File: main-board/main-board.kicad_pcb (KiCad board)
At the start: 2 copper layers, 89.8 x 61.6 mm, 62 parts, among them J1 16-bit, J2 7-12V, Q11 MBT3904DW1, Q12 MBT3904DW1, Q13 MBT3904DW1, Q14 MBT3904DW1, Q15 MBT3904DW1, Q16 MBT3904DW1, Q17 MBT3904DW1, Q18 MBT3904DW1, U1 CD40106BM96, U2 CD4024BM96, U3 CD4040BNSR, U4 27C256, U5 CD4028BM96, U6 KA78M05_TO252

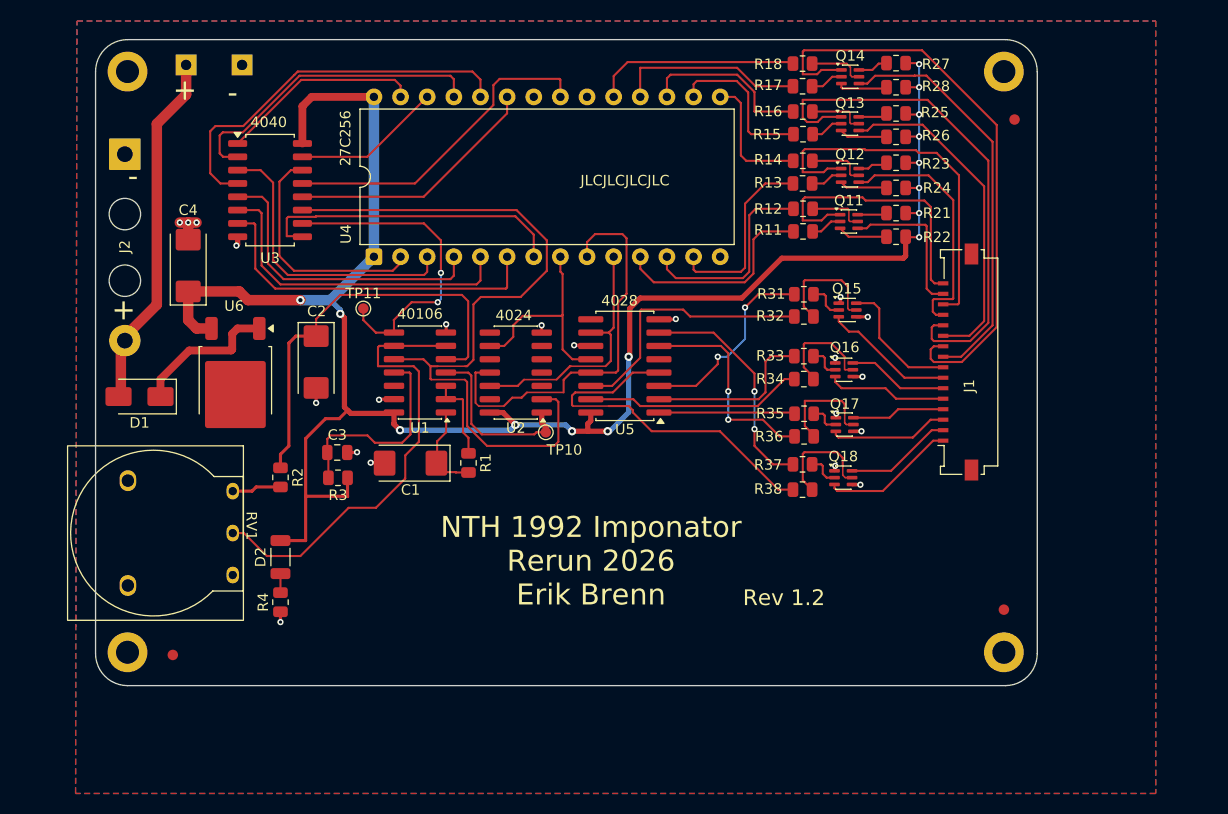
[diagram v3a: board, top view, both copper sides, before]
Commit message: new biasing and fixed footprints, shrinked pcb
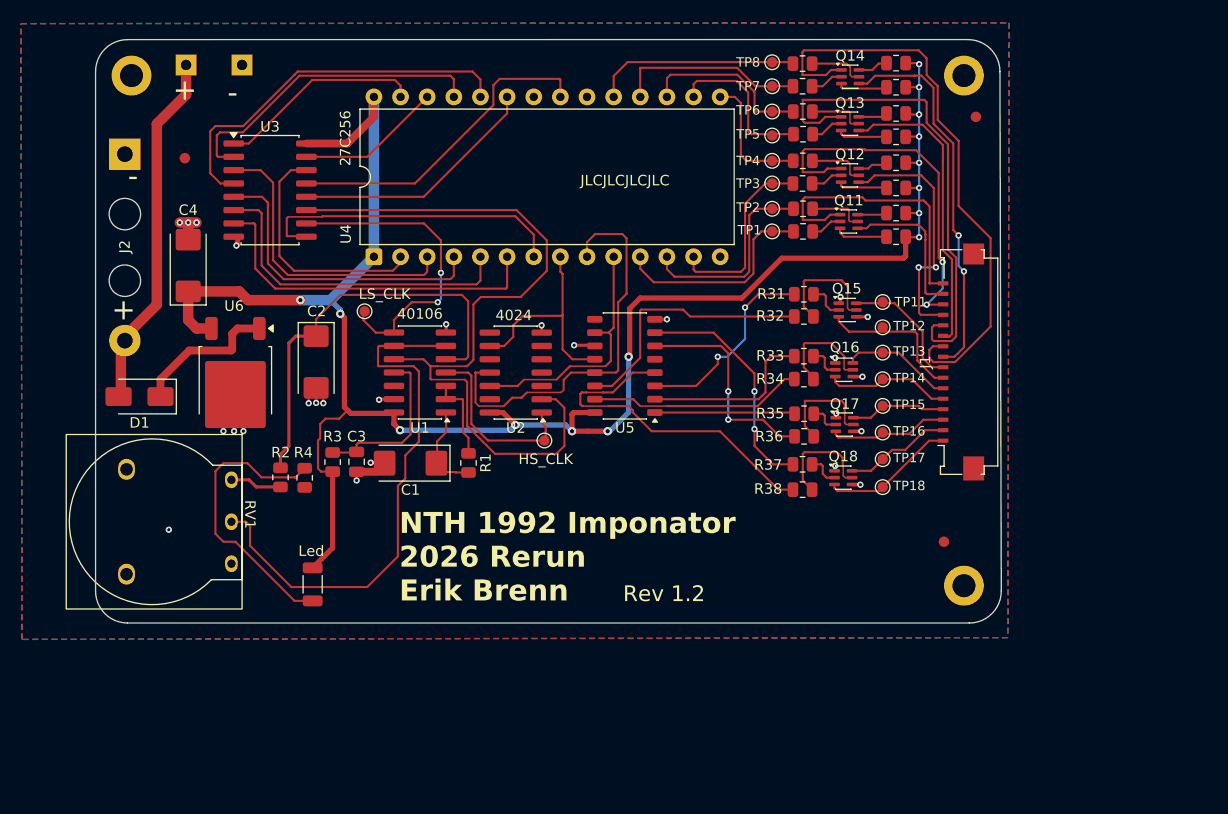
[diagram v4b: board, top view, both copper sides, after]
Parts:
- removed MH4: M3, MountingHole:MountingHole_2.2mm_M2_DIN965_Pad
- removed TP10: TestPoint, kicad-ezee-footprints:TestPoint_Pad_D1.0mm
- added TP1: TestPoint_Small, TestPoint:TestPoint_Pad_D1.0mm, F.Cu at (164.1, 75.9)
- added TP12: TestPoint_Small, TestPoint:TestPoint_Pad_D1.0mm, F.Cu at (174.6, 85.1)
- added TP13: TestPoint_Small, TestPoint:TestPoint_Pad_D1.0mm, F.Cu at (174.6, 87.5)
- added TP14: TestPoint_Small, TestPoint:TestPoint_Pad_D1.0mm, F.Cu at (174.6, 90.0)
- added TP15: TestPoint_Small, TestPoint:TestPoint_Pad_D1.0mm, F.Cu at (174.6, 92.6)
- added TP16: TestPoint_Small, TestPoint:TestPoint_Pad_D1.0mm, F.Cu at (174.6, 95.1)
- added TP17: TestPoint_Small, TestPoint:TestPoint_Pad_D1.0mm, F.Cu at (174.6, 97.7)
- added TP18: TestPoint_Small, TestPoint:TestPoint_Pad_D1.0mm, F.Cu at (174.6, 100.3)
- added TP2: TestPoint_Small, TestPoint:TestPoint_Pad_D1.0mm, F.Cu at (164.1, 73.8)
- added TP3: TestPoint_Small, TestPoint:TestPoint_Pad_D1.0mm, F.Cu at (164.1, 71.4)
- added TP4: TestPoint_Small, TestPoint:TestPoint_Pad_D1.0mm, F.Cu at (164.1, 69.2)
- added TP5: TestPoint_Small, TestPoint:TestPoint_Pad_D1.0mm, F.Cu at (164.1, 66.8)
- added TP50: HS_CLK, kicad-ezee-footprints:TestPoint_Pad_D1.0mm, F.Cu at (142.4, 95.9)
- added TP51: LS_CLK, kicad-ezee-footprints:TestPoint_Pad_D1.0mm, F.Cu at (125.2, 83.6)
- added TP6: TestPoint_Small, TestPoint:TestPoint_Pad_D1.0mm, F.Cu at (164.1, 64.5)
- added TP7: TestPoint_Small, TestPoint:TestPoint_Pad_D1.0mm, F.Cu at (164.1, 62.1)
- added TP8: TestPoint_Small, TestPoint:TestPoint_Pad_D1.0mm, F.Cu at (164.1, 59.8)
- D2: value LED -> Led
- J1: footprint Connector_FFC-FPC:Molex_200528-0160_1x16-1MP_P1.00mm_Horizontal -> kicad-ezee-footprints:FPC_1x16-P1.00mm_Horizontal
- R11, R12, R13, R14, R15, R16, R17, R18: value 8.2k -> 20k
- R21, R22, R23, R24, R25, R26, R27, R28: value 120 -> 270
- R31, R32, R33, R34, R35, R36, R37, R38: value 2.7k -> 5.2k
- TP11: value TestPoint -> TestPoint_Small; footprint kicad-ezee-footprints:TestPoint_Pad_D1.0mm -> TestPoint:TestPoint_Pad_D1.0mm
- U3: footprint Package_SO:SOP-16_4.4x10.4mm_P1.27mm -> Package_SO:SO-16_5.3x10.2mm_P1.27mm
- U5: footprint Package_SO:SOIC-16W_5.3x10.2mm_P1.27mm -> Package_SO:JEITA_SOIC-16_3.9x9.9mm_P1.27mm
- moved MH2 96.9 mm to (182.4, 61.1)
- moved TP11 49.5 mm to (174.6, 82.7)
- moved FID3 47.4 mm to (108.1, 69.0)
- moved R4 12.1 mm to (119.5, 99.4)
- moved FID2 8.64 mm to (180.5, 105.5)
- moved MH3 7.41 mm to (182.4, 109.7)
- moved D2 4.02 mm to (120.3, 109.6)
- moved FID1 3.69 mm to (183.5, 65.0)
- moved C3 2.05 mm to (124.5, 97.9), turned to -90 degrees
- moved R3 1.58 mm to (122.2, 97.9), turned to 90 degrees
- moved RV1 1.09 mm to (112.5, 99.6)
- moved MH1 0.54 mm to (103.0, 61.1)
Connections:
- net Net-(U2-Q0) renamed /A0
- net Net-(U2-Q1) renamed /A1
- net Net-(U2-Q2) renamed /A2
- net Net-(U2-~{CLK}) renamed /HS_CLK
- net Net-(U3-Q0) renamed /A3
- net Net-(U3-Q1) renamed /A4
- net Net-(U3-Q10) renamed /A13
- net Net-(U3-Q11) renamed /A15
- net Net-(U3-Q2) renamed /A5
- net Net-(U3-Q3) renamed /A6
- net Net-(U3-Q4) renamed /A7
- net Net-(U3-Q5) renamed /A8
- net Net-(U3-Q6) renamed /A9
- net Net-(U3-Q7) renamed /A10
- net Net-(U3-Q8) renamed /A11
- net Net-(U3-Q9) renamed /A12
- TP11 pad 1: Net-(U3-CLK) -> O1
- U1 pad 8: Net-(U3-CLK) -> /LS_CLK
- U3 pad 10: Net-(U3-CLK) -> /LS_CLK
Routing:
- net Net-(U3-CLK): track 30.5 -> 0.00 mm, vias 2 -> 0
- net /LS_CLK: track 0.00 -> 30.5 mm, vias 0 -> 2
- net Net-(D2-K): track 1.81 -> 27.7 mm
- net GND: track 20.7 -> 36.7 mm, vias 21 -> 26
- net Net-(RV1-Pad2): track 43.6 -> 51.7 mm
- net Net-(C3-Pad1): track 19.9 -> 16.0 mm
- net I6: track 32.0 -> 28.4 mm
- net I5: track 49.8 -> 46.3 mm
- net +5V: track 186.7 -> 183.3 mm
- net I8: track 39.1 -> 36.2 mm, vias 0 -> 2
- net Net-(U2-MR): track 73.3 -> 75.0 mm
- net Net-(U5-S7): track 34.6 -> 33.1 mm
- net O2: track 12.6 -> 14.1 mm
- net 03: track 9.61 -> 10.7 mm
- net /HS_CLK: track 16.8 -> 17.7 mm
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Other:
- board size 89.8 x 61.6 mm -> 86.4 x 55.6 mm
- board text added: "NTH 1992 Imponator 2026 Rerun Erik Brenn"
- board text removed: "NTH 1992 Imponator Rerun 2026 Erik Brenn"
